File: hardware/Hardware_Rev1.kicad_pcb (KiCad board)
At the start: 2 copper layers, 144.8 x 63.5 mm, 150 parts, among them J1 RJ45_LED_Shielded, Q1 BSS138, Q10 Q_PMOS_GSD, Q11 Q_PMOS_GSD, Q12 Q_PMOS_GSD, Q13 BSS138, Q14 BSS138, Q15 BSS138, Q16 Q_PMOS_GSD, Q17 Q_PMOS_GSD, Q18 Q_PMOS_GSD, Q19 BSS138, Q2 BSS138, Q20 BSS138, Q21 BSS138, Q22 Q_PMOS_GSD, Q23 Q_PMOS_GSD, Q24 Q_PMOS_GSD, Q3 BSS138, Q4 Q_PMOS_GSD, Q5 Q_PMOS_GSD, Q6 Q_PMOS_GSD, Q7 BSS138, Q8 BSS138, Q9 BSS138, U1 OKI, U2 Teensy4.1_DEV-16771

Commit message: Worked on heater circuits
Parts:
- Q1, Q14, Q15, Q20, Q21, Q3, Q7, Q8, Q9, R1, R11, R12, R13, R14, R15, R16, R2, R23, R24, R25, R26, R32, R33, R34, R35, R5, R51, R53, R54, R55, R56, R58, R59, R6, R61, R62: moved to B.Cu
- moved D22 350.5 mm to (200.4, 110.5), turned to 90 degrees
- moved D18 334.5 mm to (188.7, 110.5), turned to 90 degrees
- moved D23 328.6 mm to (203.3, 110.5), turned to 90 degrees
- moved D26 328.6 mm to (212.1, 110.5), turned to 90 degrees
- moved U1 325.0 mm to (199.9, 94.5), turned to -90 degrees
- moved R10 302.7 mm to (207.8, 97.0)
- moved D25 301.3 mm to (209.2, 110.5), turned to 90 degrees
- moved Q24 294.1 mm to (172.5, 75.6), turned to 180 degrees
- moved D15 292.0 mm to (180.0, 110.5), turned to 90 degrees
- moved Q1 292.0 mm to (186.6, 83.8)
- moved R46 289.7 mm to (200.4, 106.7), turned to 90 degrees
- moved D24 284.1 mm to (206.2, 110.5), turned to 90 degrees
- moved R41 279.9 mm to (185.8, 106.7), turned to 90 degrees
- moved R17 279.7 mm to (197.0, 74.7), turned to 180 degrees
- moved Q4 279.7 mm to (182.6, 75.8), turned to 180 degrees
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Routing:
- net +12V: track 1.44 -> 14.1 mm, vias 1 -> 10
- net Net-(Q12-Pad1): track 0.00 -> 6.64 mm, vias 0 -> 1
- net Net-(Q23-Pad1): track 0.00 -> 6.46 mm, vias 0 -> 1
- net Net-(Q18-Pad1): track 0.00 -> 6.46 mm, vias 0 -> 1
- net Net-(Q6-Pad1): track 0.00 -> 6.44 mm, vias 0 -> 1
- net Net-(Q24-Pad1): track 0.00 -> 6.43 mm, vias 0 -> 1
- net Net-(Q10-Pad1): track 0.00 -> 6.43 mm, vias 0 -> 1
- net Net-(Q11-Pad1): track 0.00 -> 6.34 mm, vias 0 -> 1
- net Net-(Q4-Pad1): track 0.00 -> 6.31 mm, vias 0 -> 1
- net Net-(Q16-Pad1): track 0.00 -> 6.25 mm, vias 0 -> 1
- net Heater6: track 0.00 -> 5.74 mm
- net Heater10: track 0.00 -> 5.62 mm
- net Heater9: track 0.00 -> 5.62 mm
- net Heater7: track 0.00 -> 5.62 mm
- net Heater4: track 0.00 -> 5.61 mm
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- added copper zone on F.Cu, net /H10
- added copper zone on F.Cu, net /H11
- added copper zone on F.Cu, net /H12
- added copper zone on F.Cu, net /H2
- added copper zone on F.Cu, net /H3
- added copper zone on F.Cu, net /H4
- added copper zone on F.Cu, net /H5
- added copper zone on F.Cu, net /H6
- added copper zone on F.Cu, net /H7
- added copper zone on F.Cu, net /H8
- added copper zone on F.Cu, net /H9
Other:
- board size 144.8 x 63.5 mm -> 144.8 x 76.2 mm
- board text added: "12V"
- board text added: "3.3V"

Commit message: Finished components + Traces
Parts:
- added G***: LOGO, MRDT_Silkscreens:z_sig_Grant_Brinker_30mmx7.3, F.Cu at (202.4, 85.1)
- added G***: LOGO, MRDT_Silkscreens:0_MRDT_Logo_10mm, F.Cu at (93.5, 86.6)
- Q13, Q19, R21, R22, R30, R31, R57, R60: moved to B.Cu
- moved D12 373.3 mm to (217.3, 77.6)
- moved Q19 311.3 mm to (217.0, 83.8)
- moved Q22 310.4 mm to (213.1, 75.6), turned to 180 degrees
- moved Q13 298.6 mm to (206.9, 83.8)
- moved R57 297.6 mm to (202.6, 82.8)
- moved Conn37 290.9 mm to (209.8, 119.9), turned to 180 degrees
- moved Conn30 286.4 mm to (177.8, 119.9), turned to 180 degrees
- moved R30 284.8 mm to (212.7, 80.0)
- moved Conn31 278.5 mm to (199.1, 119.9), turned to 180 degrees
- moved Conn29 276.2 mm to (156.5, 119.9), turned to 180 degrees
- moved R21 274.7 mm to (202.6, 80.0)
- moved Conn35 271.6 mm to (167.1, 119.9), turned to 180 degrees
- moved Conn34 266.4 mm to (145.8, 119.9), turned to 180 degrees
- moved Conn36 266.3 mm to (188.5, 119.9), turned to 180 degrees
- moved D9 265.6 mm to (207.1, 77.6)
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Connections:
- U2 pad 0: Overheat10 -> Overheat12
- U2 pad 1: Overheat9 -> Overheat11
- U2 pad 2: Overheat8 -> Overheat10
- U2 pad 22: Overheat11 -> Overheat2
- U2 pad 23: Overheat12 -> Overheat1
- U2 pad 3: Overheat7 -> Overheat9
- U2 pad 4: Overheat6 -> Overheat8
- U2 pad 5: Overheat5 -> Overheat7
- U2 pad 6: Overheat4 -> Overheat6
- U2 pad 7: Overheat3 -> Overheat5
- U2 pad 8: Overheat2 -> Overheat4
- U2 pad 9: Overheat1 -> Overheat3
- U2 pad R-: (no net) -> R-
- U2 pad T-: (no net) -> T-
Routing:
- net +3V3: track 0.00 -> 296.6 mm, vias 0 -> 1
- net Heater12: track 0.00 -> 92.8 mm
- net Heater11: track 0.00 -> 84.5 mm
- net LED: track 0.00 -> 77.6 mm
- net Heater10: track 5.62 -> 76.1 mm
- net Heater9: track 5.62 -> 70.3 mm
- net T-: track 0.00 -> 59.7 mm
- net T+: track 0.00 -> 59.6 mm
- net R+: track 0.00 -> 57.5 mm
- net R-: track 0.00 -> 57.4 mm
- net Temp12: track 0.00 -> 57.0 mm
- net Heater8: track 5.61 -> 62.0 mm
- net Overheat12: track 0.00 -> 52.8 mm
- net Overheat11: track 0.00 -> 52.4 mm
- net Overheat10: track 0.00 -> 52.1 mm
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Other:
- outline, holes or cut-outs redrawn
- board text added: "1"
- board text added: "10"
- board text added: "11"
- board text added: "12"
- board text added: "2"
- board text added: "3"
- board text added: "4"
- board text added: "5"
- board text added: "6"
- board text added: "7"
- board text added: "8"
- board text added: "9"
- board text added: "H1"
- board text added: "H10"
- board text added: "H11"
- board text added: "H2"
- board text added: "H3"
- board text added: "H4"
- board text added: "H5"
- board text added: "H6"
- board text added: "H7"
- board text added: "H8"
- board text added: "H9"
- board text added: "OVER HEAT"
- board text added: "Science Heater Board, Rev2 Mars Rover Design Team Missouri S&T, 2023 Grant Brinker"

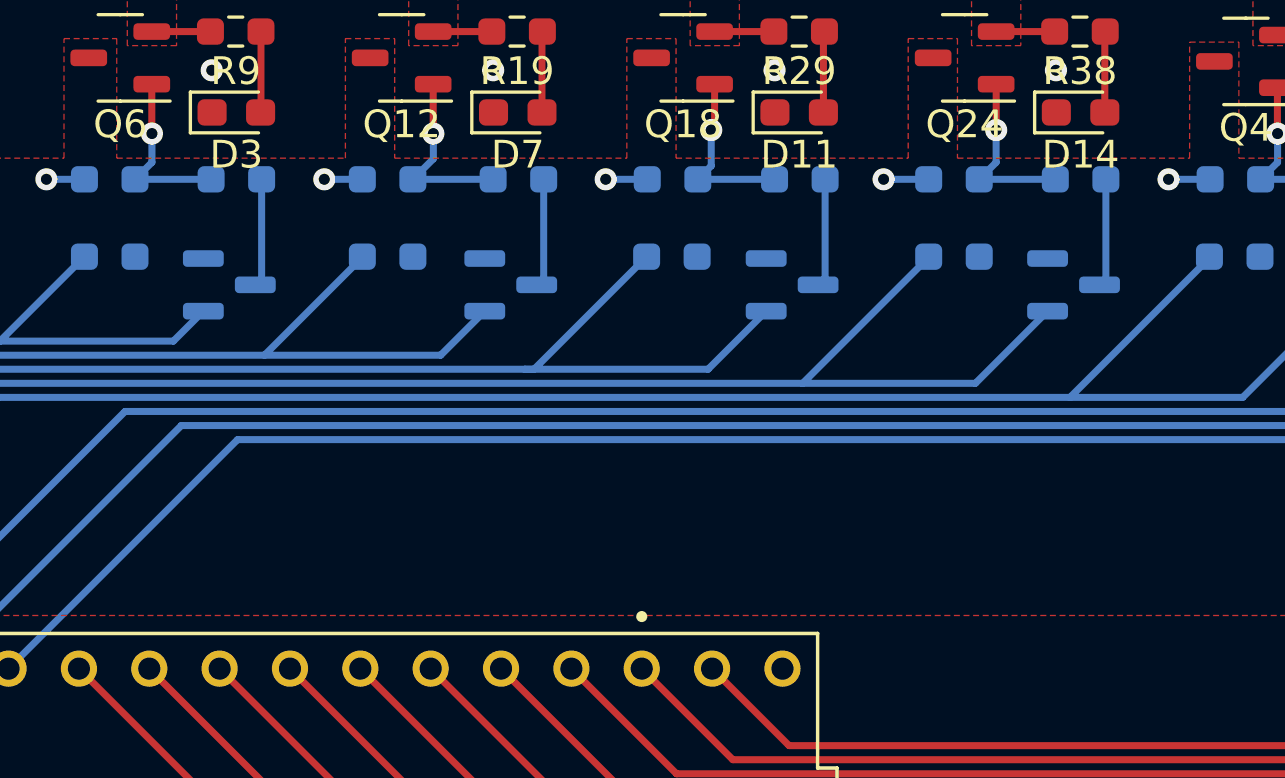
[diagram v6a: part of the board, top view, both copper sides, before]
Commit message: Added Helios logo
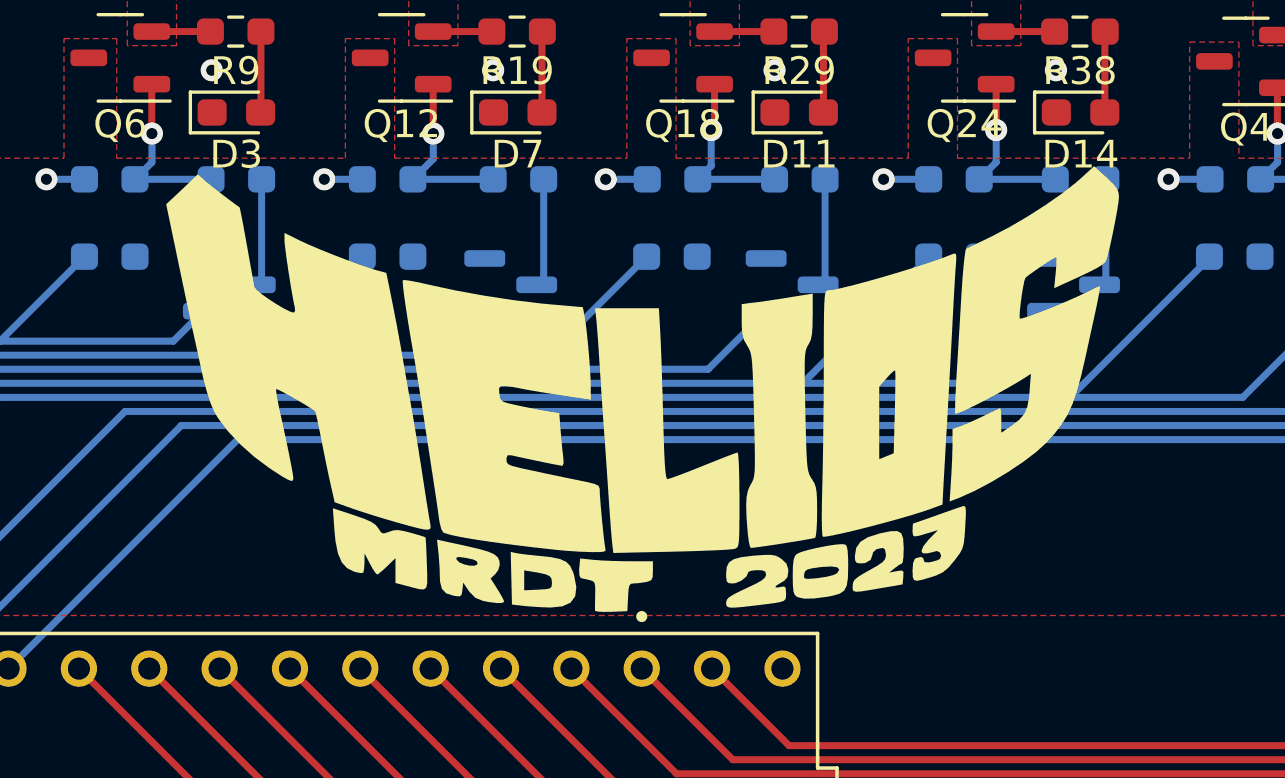
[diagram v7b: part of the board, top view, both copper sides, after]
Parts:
- added G***: LOGO, MRDT_Silkscreens:zz_Helios_Logo_Short_1.4inx0.65in, F.Cu at (160.7, 87.6)
